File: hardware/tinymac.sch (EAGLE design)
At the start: 29 parts, among them IC1 LPC1114FN28, J1 ZX62-B-5PA, SW1 TACT_SW, SW2 TACT_SW, SW3 TACT_SW, SW4 TACT_SW, SW5 TACT_SW, T1 TA48M033F

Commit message: add screw hole
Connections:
- removed net +3.3V_TGT: C3.1, IC1.AVIN
- net +3.3V: now also C3.1, IC1.AVIN
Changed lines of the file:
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@@
 <wire x1="35.56" y1="152.4" x2="35.56" y2="162.56" width="0.1524" layer="91"/>
+</segment>
+<segment>
+<pinref part="IC1" gate="G$1" pin="AVIN"/>
+<wire x1="154.94" y1="114.3" x2="154.94" y2="116.84" width="0.1524" layer="91"/>
+<wire x1="154.94" y1="116.84" x2="148.082" y2="116.84" width="0.1524" layer="91"/>
+<wire x1="148.082" y1="116.84" x2="101.6" y2="116.84" width="0.1524" layer="91"/>
+<wire x1="101.6" y1="116.84" x2="101.6" y2="121.92" width="0.1524" layer="91"/>
+<pinref part="U$5" gate="G$1" pin="+3.3V"/>
+<pinref part="C3" gate="G$1" pin="1"/>
+<junction x="148.082" y="116.84"/>
 </segment>
 </net>
@@
 </segment>
 </net>
-<net name="+3.3V_TGT" class="0">
-<segment>
-<pinref part="IC1" gate="G$1" pin="AVIN"/>
-<wire x1="154.94" y1="114.3" x2="154.94" y2="116.84" width="0.1524" layer="91"/>
-<wire x1="154.94" y1="116.84" x2="148.082" y2="116.84" width="0.1524" layer="91"/>
-<wire x1="148.082" y1="116.84" x2="101.6" y2="116.84" width="0.1524" layer="91"/>
-<wire x1="101.6" y1="116.84" x2="101.6" y2="121.92" width="0.1524" layer="91"/>
-<pinref part="U$5" gate="G$1" pin="+3.3V"/>
-<pinref part="C3" gate="G$1" pin="1"/>
-<junction x="148.082" y="116.84"/>
-</segment>
-</net>

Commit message: replace capacitor C2
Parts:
- C2: device maclock:CAPACITOR50 -> tinymac:CPOL-EUE2.5-5
- renumbered C5 to C4
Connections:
- net +3.3V: now also C2.+; no longer C2.1
- net GND: now also C2.-; no longer C2.2
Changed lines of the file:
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@@
 <part name="T1" library="tinymac" deviceset="TA48M033F" device=""/>
 <part name="C1" library="tinymac" deviceset="CAPACITOR" device="50" value="0.1uF"/>
-<part name="C2" library="maclock" deviceset="CAPACITOR" device="50" value="47uF"/>
+<part name="C2" library="tinymac" deviceset="CPOL-EU" device="E2.5-5" value="47uF"/>
 <part name="GND1" library="maclock" deviceset="GND" device=""/>
 <part name="GND2" library="maclock" deviceset="GND" device=""/>
@@
 <part name="R4" library="tinymac" deviceset="REGISTOR" device="2V" value="8.2K"/>
 <part name="R5" library="tinymac" deviceset="REGISTOR" device="2V" value="24K"/>
-<part name="C5" library="maclock" deviceset="CAPACITOR" device="50" value="0.1uF"/>
+<part name="C4" library="maclock" deviceset="CAPACITOR" device="50" value="0.1uF"/>
 <part name="U$4" library="tinymac" deviceset="+3.3V" device=""/>
 <part name="GND5" library="maclock" deviceset="GND" device=""/>
@@
 <instance part="R4" gate="G$1" x="35.56" y="109.22" rot="R90"/>
 <instance part="R5" gate="G$1" x="35.56" y="99.06" rot="R90"/>
-<instance part="C5" gate="G$1" x="224.282" y="114.3"/>
+<instance part="C4" gate="G$1" x="224.282" y="114.3"/>
 <instance part="U$4" gate="G$1" x="241.3" y="124.46"/>
 <instance part="GND5" gate="1" x="241.3" y="86.36"/>
@@
 <segment>
 <wire x1="93.98" y1="12.7" x2="93.98" y2="17.78" width="0.1524" layer="91"/>
-<pinref part="C2" gate="G$1" pin="2"/>
+<pinref part="C2" gate="G$1" pin="-"/>
 <pinref part="GND4" gate="1" pin="GND"/>
 </segment>
@@
 <wire x1="241.3" y1="86.36" x2="241.3" y2="109.22" width="0.1524" layer="91"/>
 <junction x="241.3" y="109.22"/>
-<pinref part="C5" gate="G$1" pin="2"/>
+<pinref part="C4" gate="G$1" pin="2"/>
 <junction x="224.282" y="109.22"/>
 <wire x1="220.98" y1="109.22" x2="220.98" y2="114.3" width="0.1524" layer="91"/>
@@
 <segment>
 <pinref part="U$2" gate="G$1" pin="+3.3V"/>
-<pinref part="C2" gate="G$1" pin="1"/>
+<pinref part="C2" gate="G$1" pin="+"/>
 <wire x1="93.98" y1="30.48" x2="101.6" y2="30.48" width="0.1524" layer="91"/>
 <wire x1="93.98" y1="25.4" x2="93.98" y2="30.48" width="0.1524" layer="91"/>
@@
 <wire x1="241.3" y1="116.84" x2="248.92" y2="116.84" width="0.1524" layer="91"/>
 <junction x="241.3" y="116.84"/>
-<pinref part="C5" gate="G$1" pin="1"/>
+<pinref part="C4" gate="G$1" pin="1"/>
 <junction x="224.282" y="116.84"/>
 <pinref part="IC1" gate="G$1" pin="VIN"/>

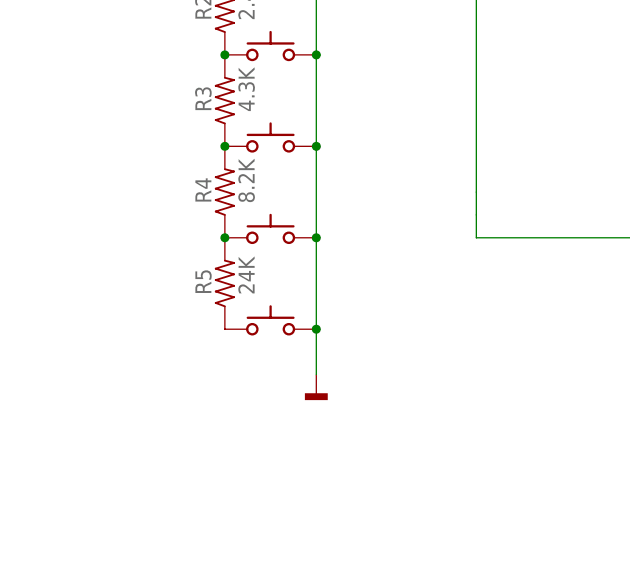
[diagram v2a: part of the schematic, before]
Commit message: move full GND to bottom layer
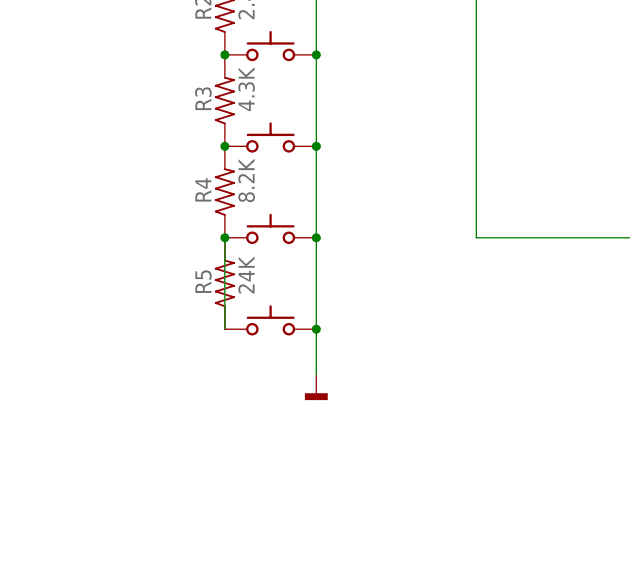
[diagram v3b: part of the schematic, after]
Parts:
- C1: device tinymac:CAPACITOR50 -> tinymac:CAPACITOR25
- C3, C4: device maclock:CAPACITOR50 -> tinymac:CAPACITOR25
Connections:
- net N$15: now also R2.1; no longer R2.2
- net N$2: now also R2.2; no longer R2.1
- net N$7: now also R5.1; no longer R5.2
- net N$8: now also R5.2; no longer R5.1
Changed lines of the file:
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@@
 <?xml version="1.0" encoding="utf-8"?>
 <!DOCTYPE eagle SYSTEM "eagle.dtd">
-<eagle version="7.0.0">
+<eagle version="7.1.0">
 <drawing>
 <settings>
@@
 <part name="J1" library="macklock" deviceset="ZX62-B-5PA" device=""/>
 <part name="T1" library="tinymac" deviceset="TA48M033F" device=""/>
-<part name="C1" library="tinymac" deviceset="CAPACITOR" device="50" value="0.1uF"/>
+<part name="C1" library="tinymac" deviceset="CAPACITOR" device="25" value="0.1uF"/>
 <part name="C2" library="tinymac" deviceset="CPOL-EU" device="E2.5-5" value="47uF"/>
 <part name="GND1" library="maclock" deviceset="GND" device=""/>
@@
 <part name="R4" library="tinymac" deviceset="REGISTOR" device="2V" value="8.2K"/>
 <part name="R5" library="tinymac" deviceset="REGISTOR" device="2V" value="24K"/>
-<part name="C4" library="maclock" deviceset="CAPACITOR" device="50" value="0.1uF"/>
+<part name="C4" library="tinymac" deviceset="CAPACITOR" device="25" value="0.1uF"/>
 <part name="U$4" library="tinymac" deviceset="+3.3V" device=""/>
 <part name="GND5" library="maclock" deviceset="GND" device=""/>
@@
 <part name="JP1" library="maclock2" deviceset="PINHD-1X6" device="_2.54"/>
 <part name="S1" library="tinymac" deviceset="PKM13EPYH4000" device=""/>
-<part name="C3" library="maclock" deviceset="CAPACITOR" device="50" value="0.1uF"/>
+<part name="C3" library="tinymac" deviceset="CAPACITOR" device="25" value="0.1uF"/>
 <part name="U$5" library="tinymac" deviceset="+3.3V" device=""/>
 </parts>
@@
 <pinref part="SW1" gate="G$1" pin="P$1"/>
 <pinref part="R1" gate="G$1" pin="1"/>
-<pinref part="R2" gate="G$1" pin="2"/>
+<pinref part="R2" gate="G$1" pin="1"/>
 <junction x="35.56" y="134.62"/>
 <wire x1="35.56" y1="139.7" x2="35.56" y2="142.24" width="0.1524" layer="91"/>
@@
 <segment>
 <pinref part="SW2" gate="G$1" pin="P$1"/>
-<pinref part="R2" gate="G$1" pin="1"/>
+<pinref part="R2" gate="G$1" pin="2"/>
 <pinref part="R3" gate="G$1" pin="2"/>
 <junction x="35.56" y="124.46"/>
@@
 <pinref part="SW4" gate="G$1" pin="P$1"/>
 <pinref part="R4" gate="G$1" pin="1"/>
+<pinref part="R5" gate="G$1" pin="1"/>
+<junction x="35.56" y="104.14"/>
+<pinref part="R5" gate="G$1" pin="1"/>
+</segment>
+</net>
+<net name="N$8" class="0">
+<segment>
+<pinref part="SW5" gate="G$1" pin="P$1"/>
 <pinref part="R5" gate="G$1" pin="2"/>
-<junction x="35.56" y="104.14"/>
-<pinref part="R5" gate="G$1" pin="2"/>
-</segment>
-</net>
-<net name="N$8" class="0">
-<segment>
-<pinref part="SW5" gate="G$1" pin="P$1"/>
-<pinref part="R5" gate="G$1" pin="1"/>
-</segment>
-</net>
+<wire x1="35.56" y1="93.98" x2="35.56" y2="104.14" width="0.1524" layer="91"/>
+</segment>
+</net>

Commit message: change DRU setting to Seeed-2layer-DRU
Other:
- note added: "Nokia 5110 LCD"
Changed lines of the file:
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@@
 <sheet>
 <plain>
+<text x="78.74" y="170.18" size="1.778" layer="97">Nokia 5110 LCD</text>
 </plain>
 <instances>

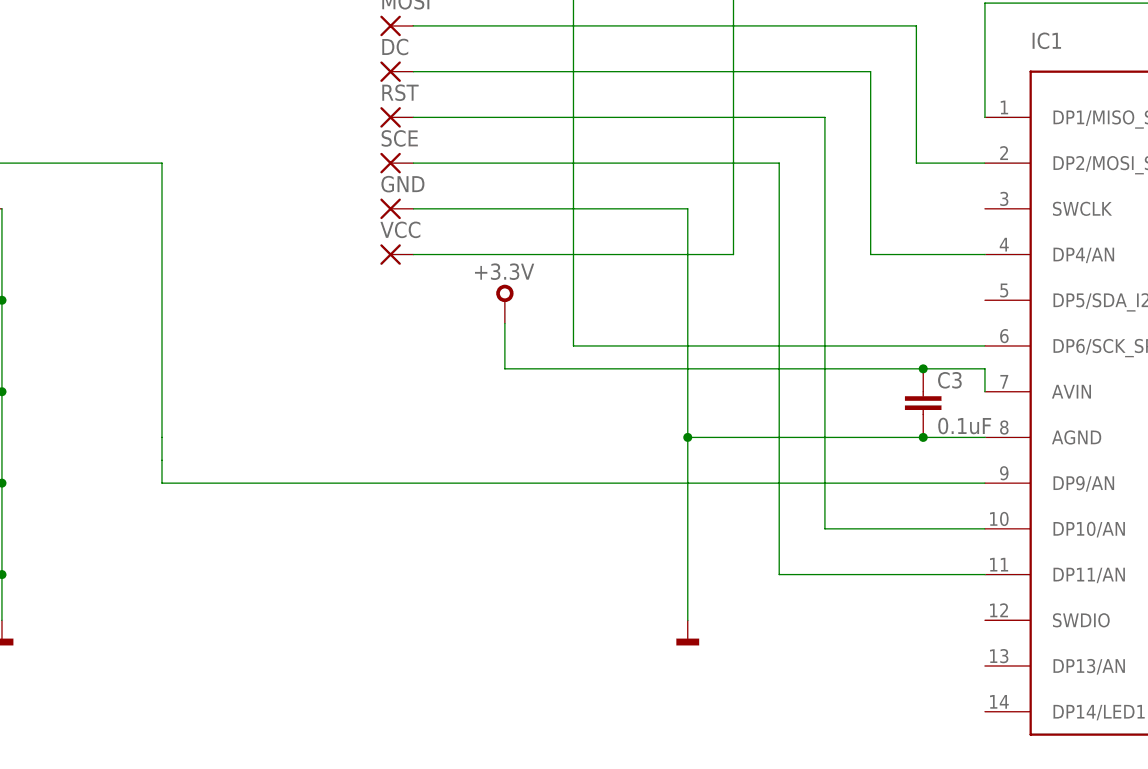
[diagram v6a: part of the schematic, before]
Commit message: apply pin setting in firmware code as schematic
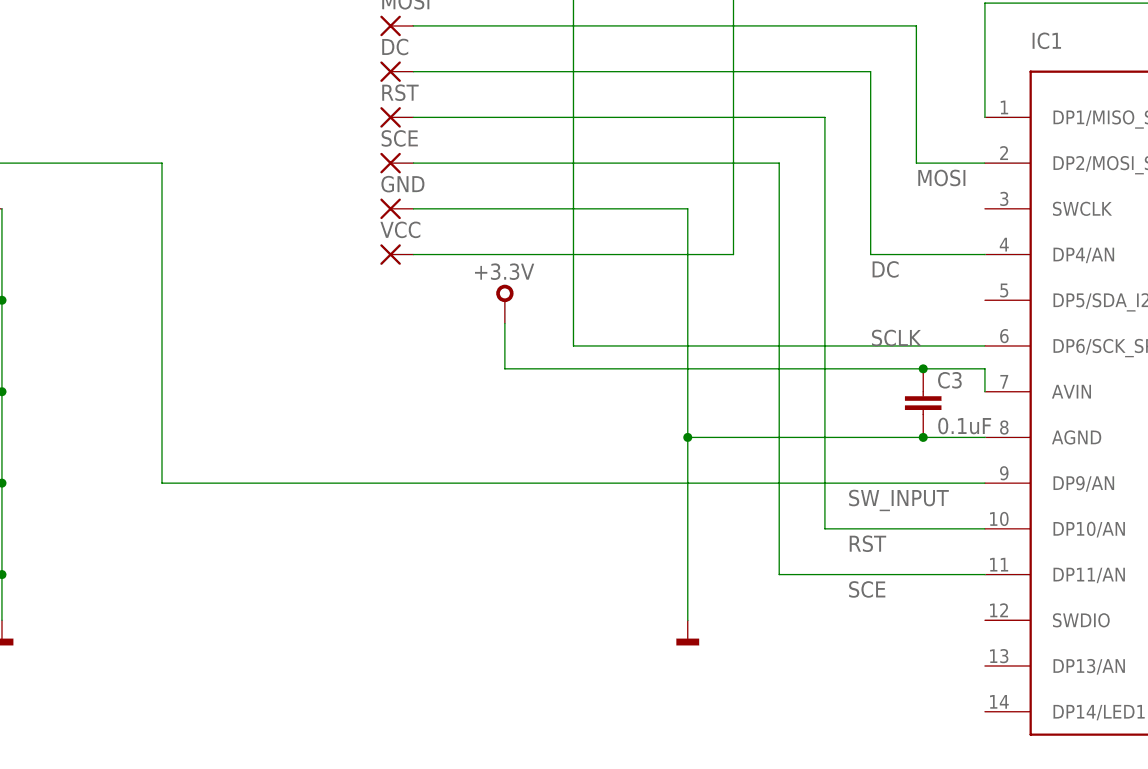
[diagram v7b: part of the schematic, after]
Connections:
- net N$10 renamed RST
- net N$12 renamed SCE
- net N$15 renamed SW_INPUT
- net N$4 renamed MOSI
- net N$5 renamed SCLK
- net N$9 renamed DC
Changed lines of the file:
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@@
 </segment>
 </net>
-<net name="N$15" class="0">
+<net name="SW_INPUT" class="0">
 <segment>
 <wire x1="35.56" y1="134.62" x2="35.56" y2="139.7" width="0.1524" layer="91"/>
@@
 <pinref part="IC1" gate="G$1" pin="DP9/AN"/>
 <wire x1="154.94" y1="104.14" x2="63.5" y2="104.14" width="0.1524" layer="91"/>
-<wire x1="63.5" y1="104.14" x2="63.5" y2="106.68" width="0.1524" layer="91"/>
-<wire x1="63.5" y1="106.68" x2="63.5" y2="109.22" width="0.1524" layer="91"/>
-<wire x1="63.5" y1="139.7" x2="63.5" y2="109.22" width="0.1524" layer="91"/>
+<wire x1="63.5" y1="139.7" x2="63.5" y2="104.14" width="0.1524" layer="91"/>
+<label x="139.7" y="101.6" size="1.778" layer="95"/>
 </segment>
 </net>
-<net name="N$4" class="0">
+<net name="MOSI" class="0">
 <segment>
 <wire x1="147.32" y1="154.94" x2="91.44" y2="154.94" width="0.1524" layer="91"/>
@@
 <pinref part="IC1" gate="G$1" pin="DP2/MOSI_SPI/PWM"/>
 <wire x1="147.32" y1="139.7" x2="154.94" y2="139.7" width="0.1524" layer="91"/>
+<label x="147.32" y="137.16" size="1.778" layer="95"/>
 </segment>
 </net>
-<net name="N$5" class="0">
+<net name="SCLK" class="0">
 <segment>
 <pinref part="IC1" gate="G$1" pin="DP6/SCK_SPI"/>
@@
 <pinref part="SCLK" gate="1" pin="P"/>
 <wire x1="91.44" y1="160.02" x2="88.9" y2="160.02" width="0.1524" layer="91"/>
+<label x="142.24" y="119.38" size="1.778" layer="95"/>
 </segment>
 </net>
@@
 </segment>
 </net>
-<net name="N$9" class="0">
+<net name="DC" class="0">
 <segment>
 <pinref part="DC" gate="1" pin="P"/>
@@
 <pinref part="IC1" gate="G$1" pin="DP4/AN"/>
 <wire x1="142.24" y1="129.54" x2="154.94" y2="129.54" width="0.1524" layer="91"/>
+<label x="142.24" y="127" size="1.778" layer="95"/>
 </segment>
 </net>
-<net name="N$10" class="0">
+<net name="RST" class="0">
 <segment>
 <pinref part="RST" gate="1" pin="P"/>
@@
 <pinref part="IC1" gate="G$1" pin="DP10/AN"/>
 <wire x1="137.16" y1="99.06" x2="154.94" y2="99.06" width="0.1524" layer="91"/>
+<label x="139.7" y="96.52" size="1.778" layer="95"/>
 </segment>
 </net>
-<net name="N$12" class="0">
+<net name="SCE" class="0">
 <segment>
 <pinref part="IC1" gate="G$1" pin="DP11/AN"/>
@@
 <pinref part="SCE" gate="1" pin="P"/>
 <wire x1="132.08" y1="139.7" x2="91.44" y2="139.7" width="0.1524" layer="91"/>
+<label x="139.7" y="91.44" size="1.778" layer="95"/>
 </segment>
 </net>

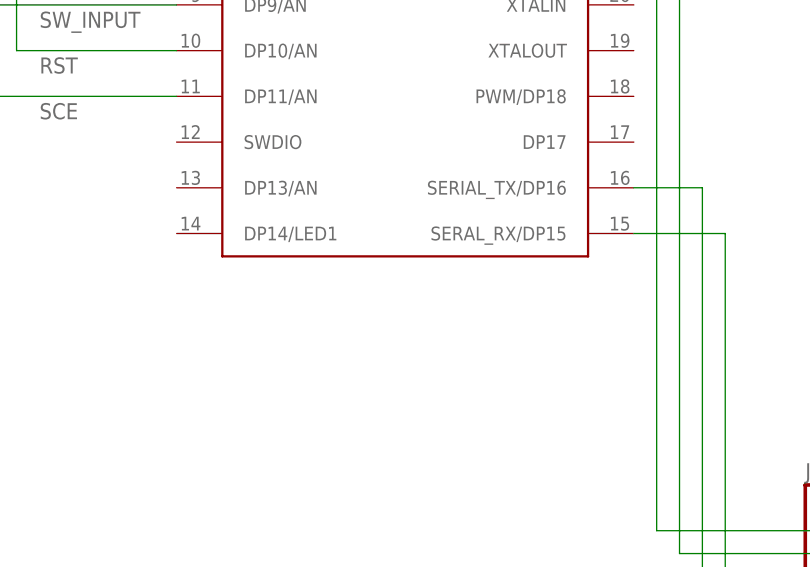
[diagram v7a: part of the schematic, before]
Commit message: add chip name notation in schematic
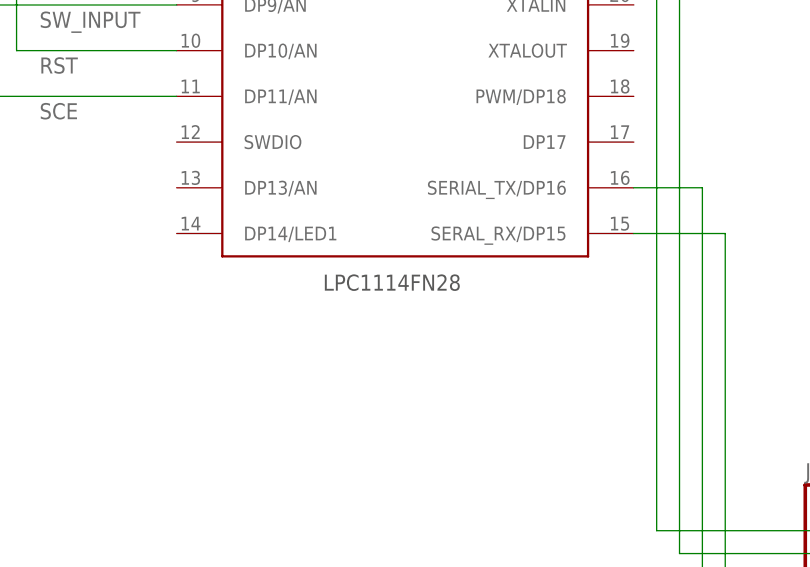
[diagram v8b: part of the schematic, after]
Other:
- note added: "LPC1114FN28"
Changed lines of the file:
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@@
 <plain>
 <text x="78.74" y="170.18" size="1.778" layer="97">Nokia 5110 LCD</text>
+<text x="171.196" y="72.39" size="1.778" layer="97">LPC1114FN28</text>
 </plain>
 <instances>
